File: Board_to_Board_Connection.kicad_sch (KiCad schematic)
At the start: 4 parts, among them J11 690367190672, J12 690367190672, J7 690367191672, J8 690367191672

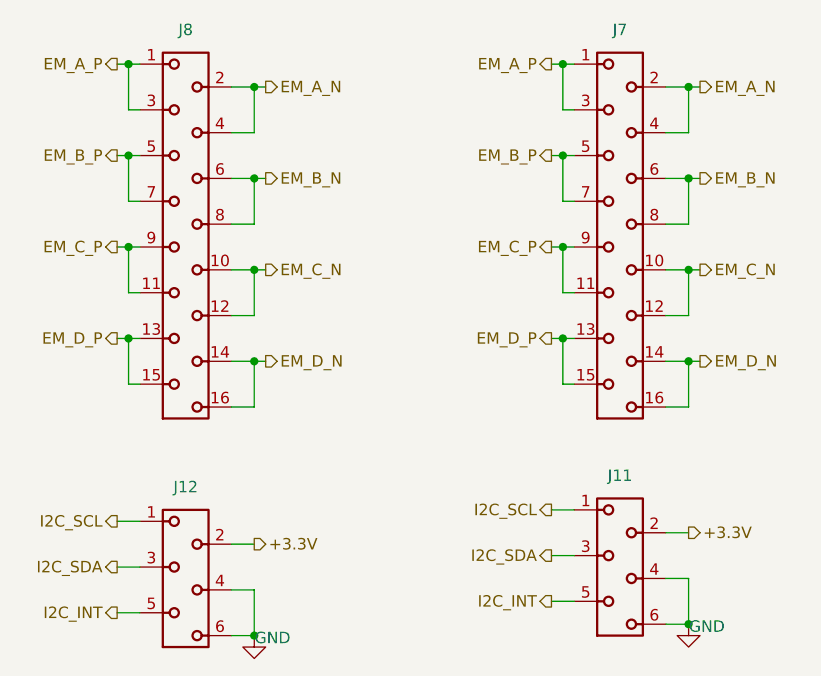
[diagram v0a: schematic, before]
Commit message: cleared some ERC errors/warnings in schematic, still one main error category to be solved
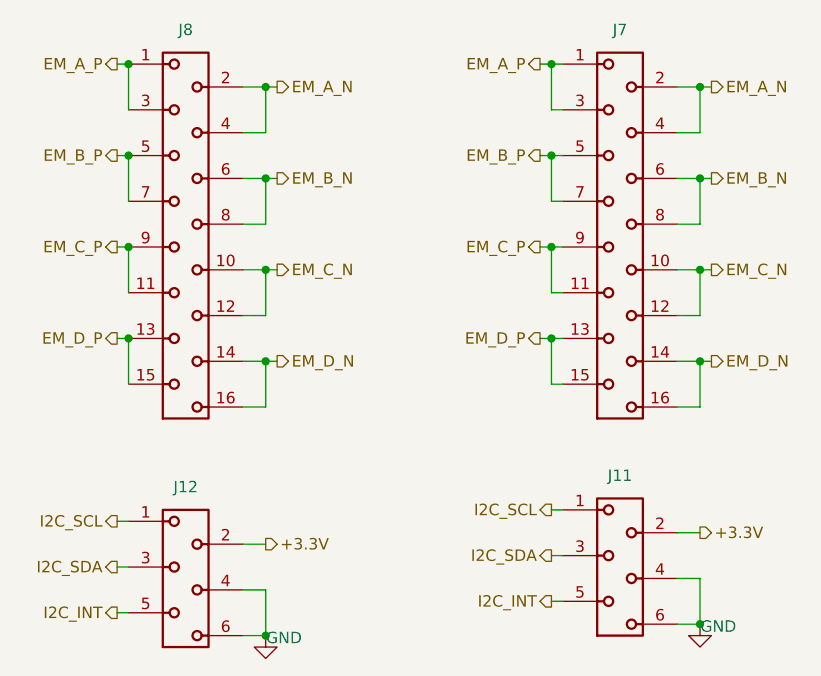
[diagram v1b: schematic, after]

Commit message: Edit symbol libraries for BOM
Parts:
- J11, J12: symbol Connector_Wurth_WR-MM:690367190672 -> Connector_Wurth_WR-MM_CUSTOM:690367190672; Contact Resistance (mohm) (none) -> 10; Part Number (none) -> 690367190672
- J7, J8: symbol Connector_Wurth_WR-MM:690367191672 -> Connector_Wurth_WR-MM_CUSTOM:690367191672; Contact Resistance (mohm) (none) -> 10; Part Number (none) -> 690367191672
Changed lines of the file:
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@@
 	)
 	(symbol
-		(lib_id "Connector_Wurth_WR-MM:690367191672")
+		(lib_id "Connector_Wurth_WR-MM_CUSTOM:690367191672")
 		(at 100.33 52.07 90)
 		(unit 1)
@@
 			)
 		)
+		(property "Contact Resistance (mohm)" "10"
+			(at 123.19 6.35 0)
+			(hide yes)
+			(show_name no)
+			(do_not_autoplace no)
+			(effects
+				(font
+					(size 1.27 1.27)
+				)
+			)
+		)
+		(property "Part Number" "690367191672"
+			(at 100.33 52.07 0)
+			(hide yes)
+			(show_name no)
+			(do_not_autoplace no)
+			(effects
+				(font
+					(size 1.27 1.27)
+				)
+			)
+		)
 		(pin "4"
 		)
@@
 	)
 	(symbol
-		(lib_id "Connector_Wurth_WR-MM:690367190672")
+		(lib_id "Connector_Wurth_WR-MM_CUSTOM:690367190672")
 		(at 100.33 88.9 90)
 		(unit 1)
@@
 			)
 		)
+		(property "Contact Resistance (mohm)" "10"
+			(at 123.19 43.18 0)
+			(hide yes)
+			(show_name no)
+			(do_not_autoplace no)
+			(effects
+				(font
+					(size 1.27 1.27)
+				)
+			)
+		)
+		(property "Part Number" "690367190672"
+			(at 100.33 88.9 0)
+			(hide yes)
+			(show_name no)
+			(do_not_autoplace no)
+			(effects
+				(font
+					(size 1.27 1.27)
+				)
+			)
+		)
 		(pin "1"
 		)
@@
 	)
 	(symbol
-		(lib_id "Connector_Wurth_WR-MM:690367191672")
+		(lib_id "Connector_Wurth_WR-MM_CUSTOM:690367191672")
 		(at 52.07 52.07 90)
 		(unit 1)
@@
 			)
 		)
+		(property "Contact Resistance (mohm)" "10"
+			(at 74.93 6.35 0)
+			(hide yes)
+			(show_name no)
+			(do_not_autoplace no)
+			(effects
+				(font
+					(size 1.27 1.27)
+				)
+			)
+		)
+		(property "Part Number" "690367191672"
+			(at 52.07 52.07 0)
+			(hide yes)
+			(show_name no)
+			(do_not_autoplace no)
+			(effects
+				(font
+					(size 1.27 1.27)
+				)
+			)
+		)
 		(pin "4"
 		)
@@
 	)
 	(symbol
-		(lib_id "Connector_Wurth_WR-MM:690367190672")
+		(lib_id "Connector_Wurth_WR-MM_CUSTOM:690367190672")
 		(at 52.07 90.17 90)
 		(unit 1)
@@
 			(hide yes)
 			(show_name no)
+			(do_not_autoplace no)
+			(effects
+				(font
+					(size 1.27 1.27)
+				)
+			)
+		)
+		(property "Contact Resistance (mohm)" "10"
+			(at 74.93 44.45 0)
+			(hide yes)
+			(show_name no)
+			(do_not_autoplace no)
+			(effects
+				(font
+					(size 1.27 1.27)
+				)
+			)
+		)
+		(property "Part Number" "690367190672"
+			(at 52.07 90.17 0)
+			(hide yes)
+			(show_name no)

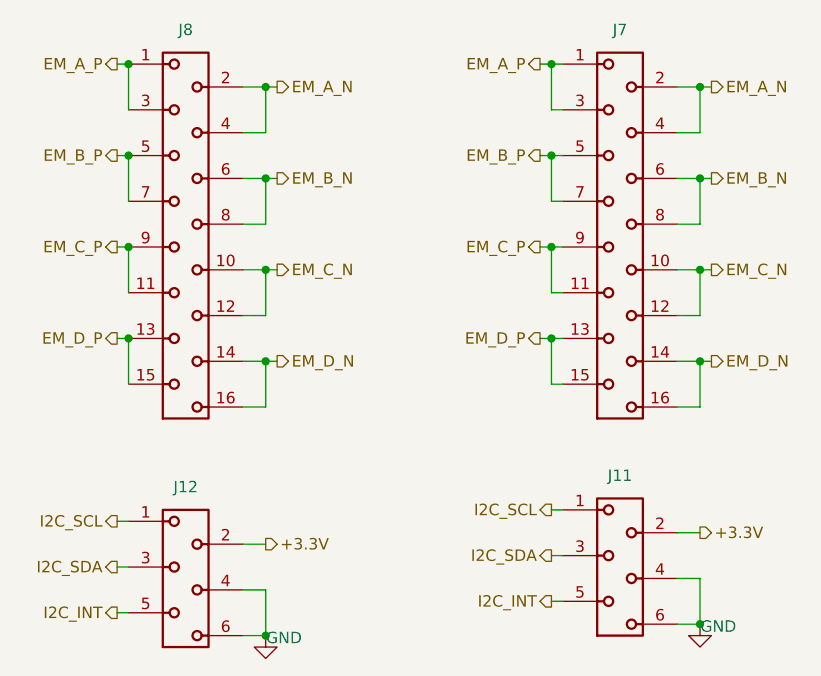
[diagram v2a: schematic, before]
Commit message: continued and finished conversion to ESP32-S3-WROOM module
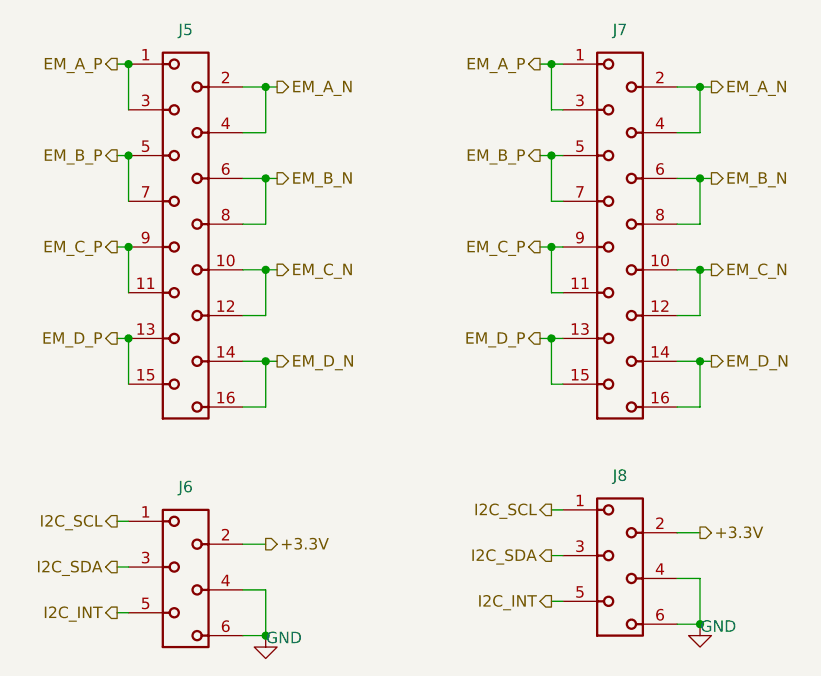
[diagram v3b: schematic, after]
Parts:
- renumbered J8 to J5, J12 to J6, J11 to J8
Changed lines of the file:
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@@
 		(dnp no)
 		(fields_autoplaced yes)
-		(property "Reference" "J11"
+		(property "Reference" "J8"
 			(at 100.33 78.74 90)
 			(show_name no)
@@
 			(project "Maglev"
 				(path "/cf460145-35f8-4019-907e-b966a2c32625/fa0f1235-f62c-4c44-92f4-296ab8f601de"
-					(reference "J11")
+					(reference "J8")
 					(unit 1)
 				)
@@
 		(dnp no)
 		(fields_autoplaced yes)
-		(property "Reference" "J8"
+		(property "Reference" "J5"
 			(at 52.07 29.21 90)
 			(show_name no)
@@
 			(project "Maglev"
 				(path "/cf460145-35f8-4019-907e-b966a2c32625/fa0f1235-f62c-4c44-92f4-296ab8f601de"
-					(reference "J8")
+					(reference "J5")
 					(unit 1)
 				)
@@
 		(dnp no)
 		(fields_autoplaced yes)
-		(property "Reference" "J12"
+		(property "Reference" "J6"
 			(at 52.07 80.01 90)
 			(show_name no)
@@
 			(project "Maglev"
 				(path "/cf460145-35f8-4019-907e-b966a2c32625/fa0f1235-f62c-4c44-92f4-296ab8f601de"
-					(reference "J12")
+					(reference "J6")
 					(unit 1)
 				)
@@
 		(in_pos_files yes)
 		(dnp no)
-		(property "Reference" "#PWR056"
+		(property "Reference" "#PWR043"
 			(at 109.22 101.6 0)
 			(hide yes)
@@
 			(project "Maglev"
 				(path "/cf460145-35f8-4019-907e-b966a2c32625/fa0f1235-f62c-4c44-92f4-296ab8f601de"
-					(reference "#PWR056")
+					(reference "#PWR043")
 					(unit 1)
 				)
@@
 		(in_pos_files yes)
 		(dnp no)
-		(property "Reference" "#PWR057"
+		(property "Reference" "#PWR042"
 			(at 60.96 102.87 0)
 			(hide yes)
@@
 			(project "Maglev"
 				(path "/cf460145-35f8-4019-907e-b966a2c32625/fa0f1235-f62c-4c44-92f4-296ab8f601de"
-					(reference "#PWR057")
+					(reference "#PWR042")
 					(unit 1)
 				)
